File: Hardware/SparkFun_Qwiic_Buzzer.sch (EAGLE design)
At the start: 45 parts, among them J2 QWIIC_RA, J3 QWIIC_RA, Q3 200mA/40V, U4 ATTINY84-ARDUINO

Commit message: replace parts from old libraries
-fids and gnd symbols
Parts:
- JP2, JP6, JP8, JP9: device SparkFun:FIDUCIALUFIDUCIAL -> SparkFun-Aesthetics:FIDUCIALUFIDUCIAL
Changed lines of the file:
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@@
 <part name="SUPPLY7" library="SparkFun-PowerSymbols" deviceset="VCC" device="" value="3.3V"/>
 <part name="LOGO1" library="SparkFun-Aesthetics" deviceset="OSHW-LOGO" device="MINI"/>
-<part name="JP2" library="SparkFun" deviceset="FIDUCIAL" device="UFIDUCIAL"/>
-<part name="JP6" library="SparkFun" deviceset="FIDUCIAL" device="UFIDUCIAL"/>
-<part name="JP8" library="SparkFun" deviceset="FIDUCIAL" device="UFIDUCIAL"/>
-<part name="JP9" library="SparkFun" deviceset="FIDUCIAL" device="UFIDUCIAL"/>
-<part name="GND8" library="SparkFun" deviceset="GND" device=""/>
+<part name="JP2" library="SparkFun-Aesthetics" deviceset="FIDUCIAL" device="UFIDUCIAL"/>
+<part name="JP6" library="SparkFun-Aesthetics" deviceset="FIDUCIAL" device="UFIDUCIAL"/>
+<part name="JP8" library="SparkFun-Aesthetics" deviceset="FIDUCIAL" device="UFIDUCIAL"/>
+<part name="JP9" library="SparkFun-Aesthetics" deviceset="FIDUCIAL" device="UFIDUCIAL"/>
+<part name="GND8" library="SparkFun-PowerSymbols" deviceset="GND" device=""/>
 <part name="SUPPLY12" library="SparkFun-PowerSymbols" deviceset="3.3V" device=""/>
 <part name="J1" library="SparkFun-Connectors" deviceset="CONN_04" device="1X04_NO_SILK"/>
 <part name="SUPPLY2" library="SparkFun-PowerSymbols" deviceset="3.3V" device=""/>
-<part name="GND7" library="SparkFun" deviceset="GND" device=""/>
+<part name="GND7" library="SparkFun-PowerSymbols" deviceset="GND" device=""/>
 <part name="C2" library="SparkFun-Capacitors" deviceset="0.1UF" device="-0402T-16V-10%" value="0.1uF"/>
 <part name="R2" library="SparkFun-Resistors" deviceset="2.2KOHM" device="-0402T-1/16W-1%" value="2.2k"/>
@@
 <part name="SUPPLY15" library="SparkFun-PowerSymbols" deviceset="3.3V" device=""/>
 <part name="SUPPLY17" library="SparkFun-PowerSymbols" deviceset="3.3V" device=""/>
-<part name="GND13" library="SparkFun" deviceset="GND" device=""/>
+<part name="GND13" library="SparkFun-PowerSymbols" deviceset="GND" device=""/>
 <part name="R3" library="SparkFun-Resistors" deviceset="10KOHM" device="-0402T-1/16W-1%" value="10k"/>
 <part name="SUPPLY18" library="SparkFun-PowerSymbols" deviceset="3.3V" device=""/>
@@
 <part name="R4" library="SparkFun-Resistors" deviceset="4.7KOHM" device="-0402T-1/16W-1%" value="4.7k"/>
 <part name="POWER" library="SparkFun-LED" deviceset="LED-RED" device="_0603-KB" value="Red"/>
-<part name="GND10" library="SparkFun" deviceset="GND" device=""/>
+<part name="GND10" library="SparkFun-PowerSymbols" deviceset="GND" device=""/>
 <part name="J5" library="SparkFun-Connectors" deviceset="CONN_01" device="PTH_NO_SILK_YES_STOP"/>
 <part name="R11" library="SparkFun-Resistors" deviceset="10KOHM" device="-0402T-1/16W-1%" value="10k"/>
@@
 <part name="PWR" library="SparkFun-Jumpers" deviceset="JUMPER-SMT_2_NC_TRACE" device="_SILK" package3d_urn="urn:adsk.eagle:package:39281/1" value="PWR_LED"/>
 <part name="SUPPLY3" library="SparkFun-PowerSymbols" deviceset="3.3V" device=""/>
-<part name="GND9" library="SparkFun" deviceset="GND" device=""/>
+<part name="GND9" library="SparkFun-PowerSymbols" deviceset="GND" device=""/>
 <part name="Q2" library="SparkFun-DiscreteSemi" deviceset="TRANS_NPN_DUAL" device="-MBT3904DW1T1"/>
 <part name="Q3" library="SparkFun-DiscreteSemi" deviceset="TRANS_PNP" device="-PMBT3906|MMBT3906L" value="200mA/40V"/>
@@
 <part name="R14" library="SparkFun-Resistors" deviceset="330OHM" device="-0603-1/10W-1%" value="330"/>
 <part name="R15" library="SparkFun-Resistors" deviceset="100OHM" device="-0603-1/10W-1%" value="100"/>
-<part name="GND1" library="SparkFun" deviceset="GND" device=""/>
+<part name="GND1" library="SparkFun-PowerSymbols" deviceset="GND" device=""/>
 <part name="J4" library="SparkFun-Connectors" deviceset="CONN_04" device="1X04_NO_SILK"/>
 <part name="H3" library="SparkFun-Hardware" deviceset="STAND-OFF" device=""/>
@@
 <part name="STATUS" library="SparkFun-LED" deviceset="LED-BLUE" device="0603" value="Blue"/>
 <part name="R6" library="SparkFun-Resistors" deviceset="2.2KOHM" device="-0402T-1/16W-1%" value="2.2k"/>
-<part name="GND2" library="SparkFun" deviceset="GND" device=""/>
+<part name="GND2" library="SparkFun-PowerSymbols" deviceset="GND" device=""/>
 <part name="STAT" library="SparkFun-Jumpers" deviceset="JUMPER-SMT_2_NC_TRACE" device="_SILK" package3d_urn="urn:adsk.eagle:package:39281/1" value="PWR_LED"/>
 <part name="R9" library="SparkFun-Resistors" deviceset="RESISTOR" device="AXIAL-0.3" value="USER"/>

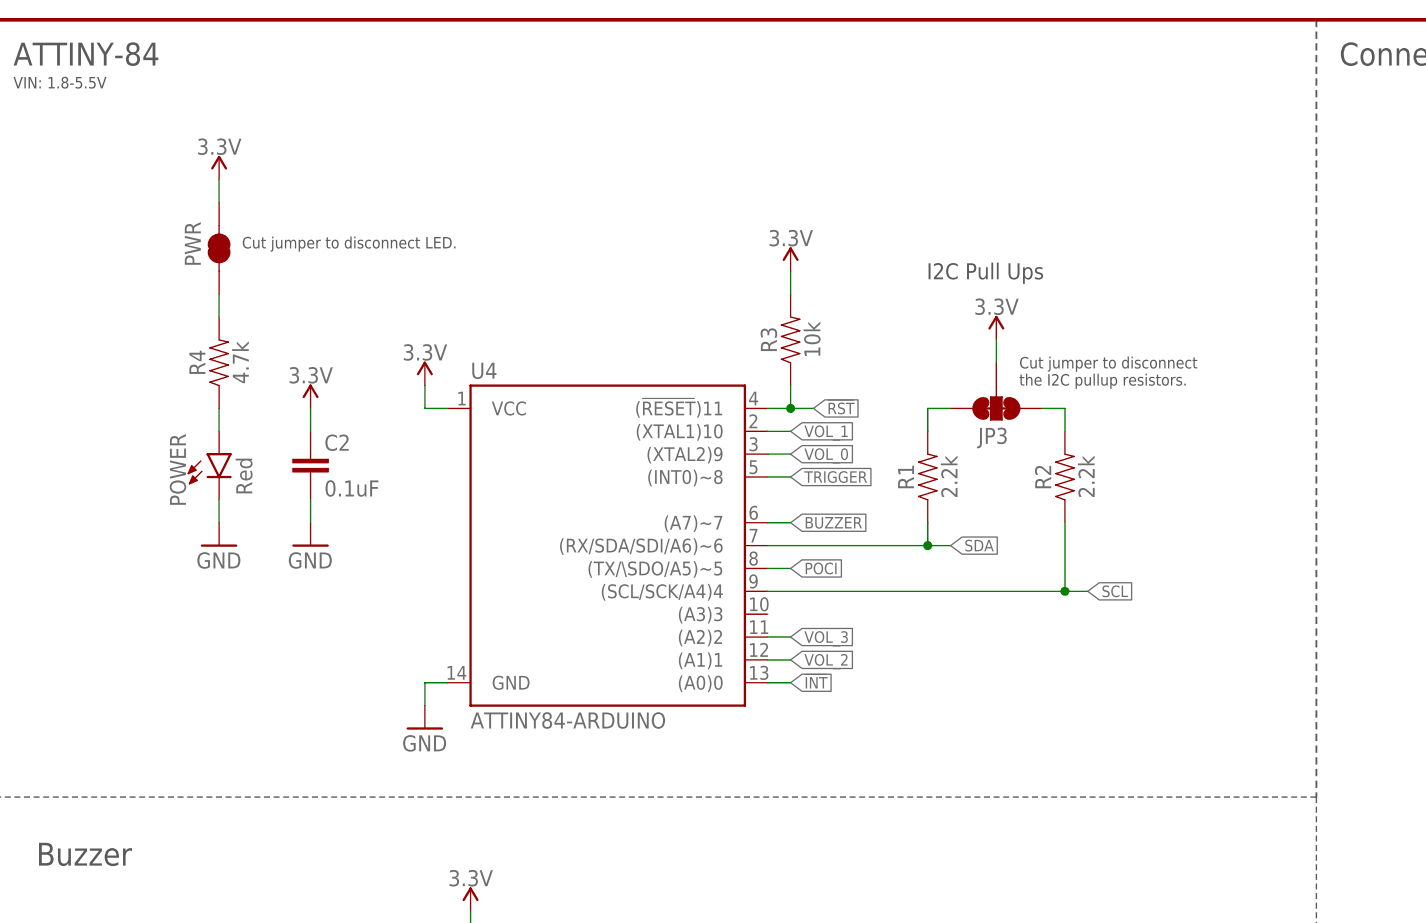
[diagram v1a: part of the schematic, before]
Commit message: default i2c address is 0x34
added note to sch.
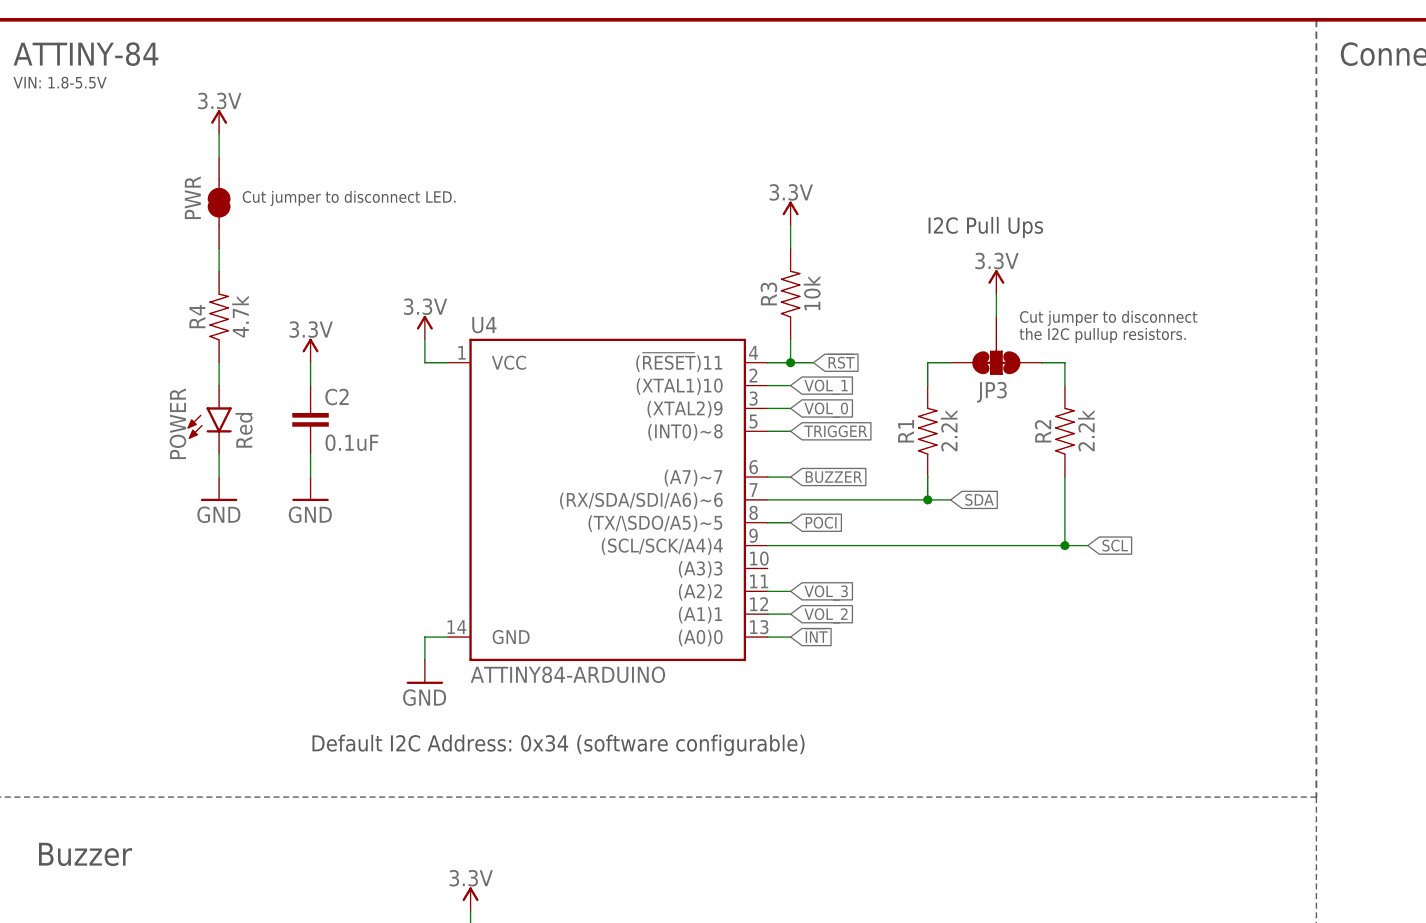
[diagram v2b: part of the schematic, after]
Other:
- note added: "Default I2C Address: 0x34 (software configurable)"
- moved on the sheet: C2, JP3, POWER, PWR, R1, R2, R3, R4, U4

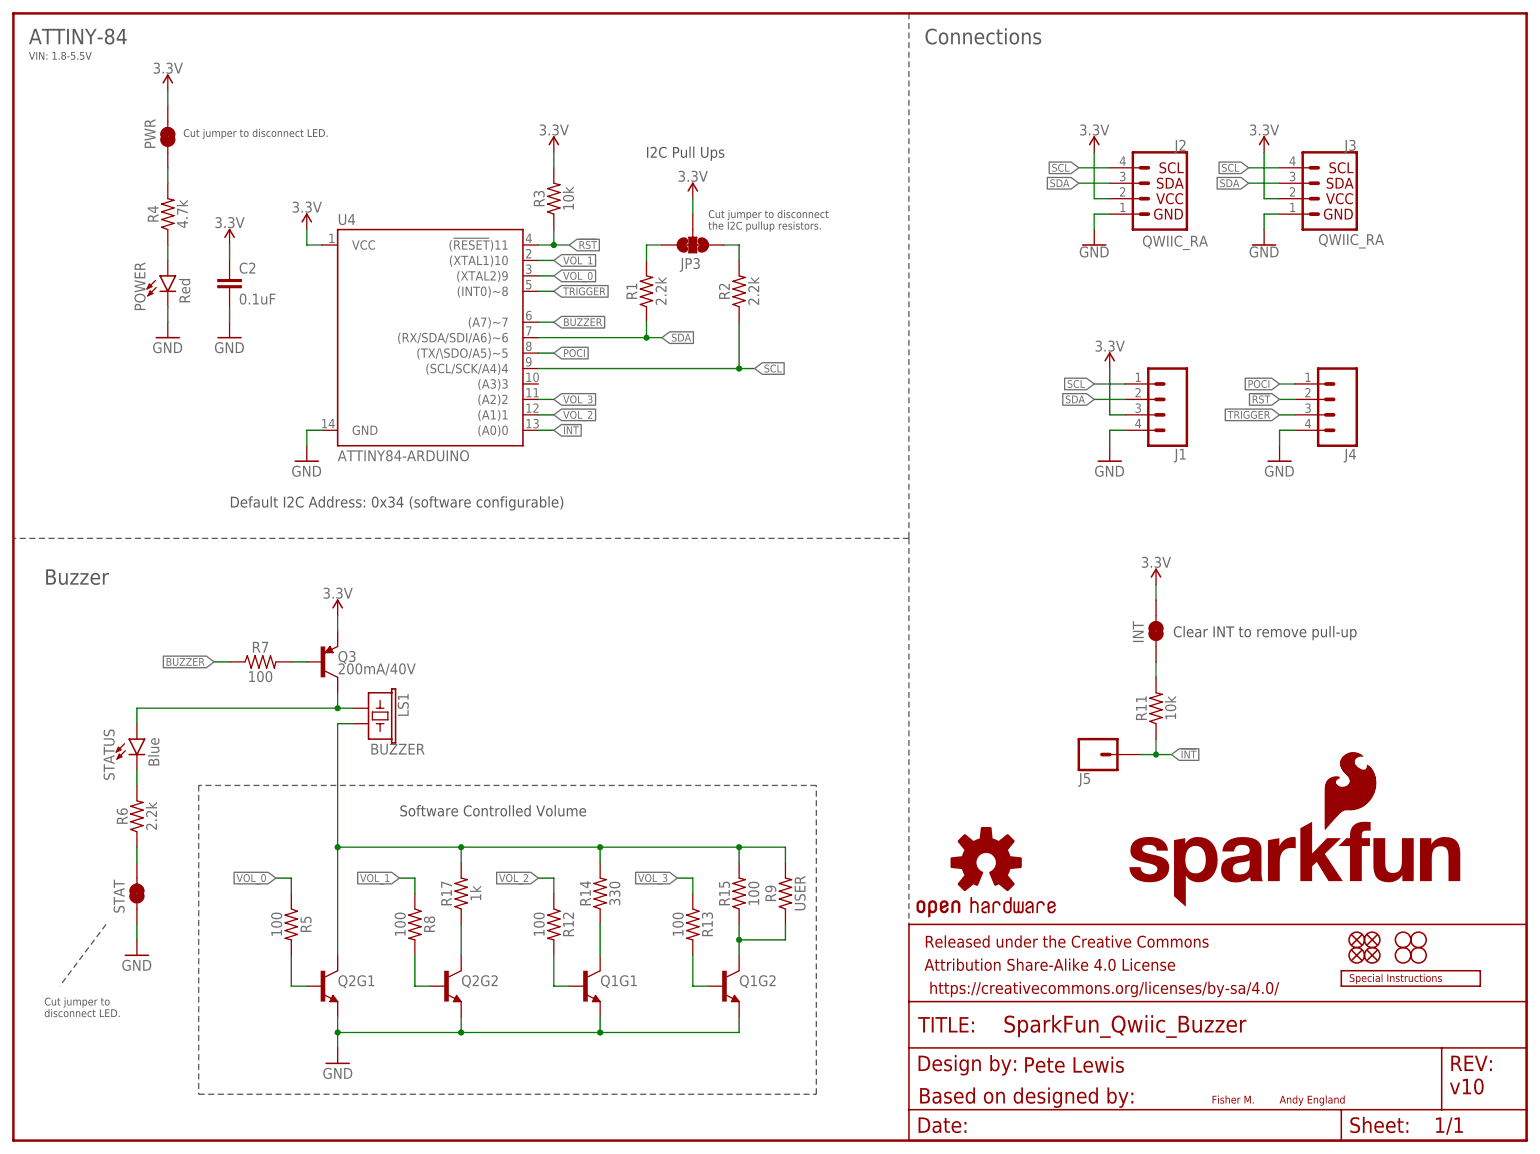
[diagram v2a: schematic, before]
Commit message: group review pre-meeting
-add flyback diode
-add tPlace lines to divide tightly packed passives
-add 10uF cap on 3V3 rail
-corrected name on I2C Jumper
-Added JP1 to allow user to easily remove R15 resistor when using USER PTH resistor for volume control
-fixes some acid traps on poci and rst headers
-increased trace from USER resistor to BJT.
-trigger net renames to have active low in the name
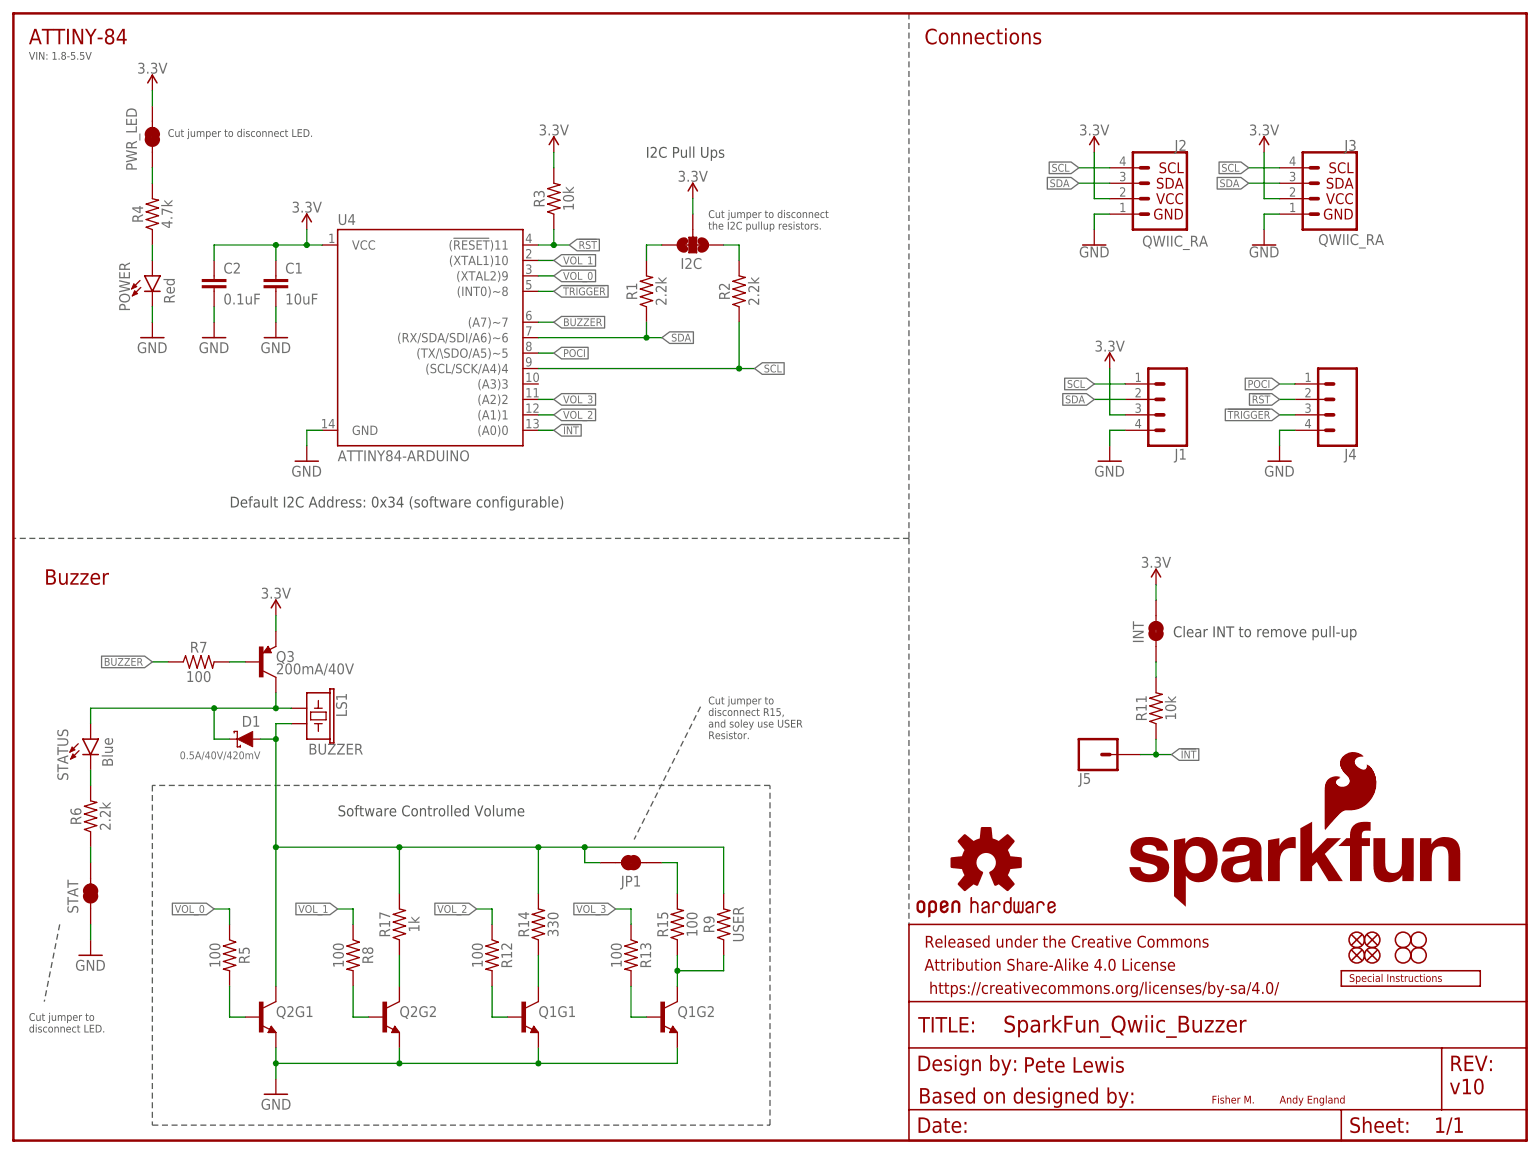
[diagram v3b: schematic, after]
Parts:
- removed PWR: PWR_LED, SparkFun-Jumpers:JUMPER-SMT_2_NC_TRACE_SILK
- added C1: 10uF, SparkFun-Capacitors:10UF-0402T-6.3V-20%
- added D1: 0.5A/40V/420mV, SparkFun-DiscreteSemi:DIODE-SCHOTTKY-PMEG4005EJ
- added JP1: JUMPER-SMT_2_NC_TRACE_SILK, SparkFun-Jumpers:JUMPER-SMT_2_NC_TRACE_SILK
- added PWR_LED: PWR_LED, SparkFun-Jumpers:JUMPER-SMT_2_NC_TRACE_SILK
- renumbered JP3 to I2C
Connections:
- net TRIGGER renamed !TRIGGER!
- new net N$16: JP1.1, R15.2
- net 3.3V: now also C1.1, PWR_LED.2; no longer PWR.2
- net GND: now also C1.2
- net N$1: now also PWR_LED.1; no longer PWR.1
- net N$4: now also D1.A, JP1.2; no longer R15.2
- net N$6: now also D1.C
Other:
- note added: "Cut jumper to disconnect R15, and soley use USER Resistor."
- moved on the sheet: C2, LS1, POWER, Q1G1, Q1G2, Q2G1, Q2G2, Q3, R12, R13, R14, R15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
